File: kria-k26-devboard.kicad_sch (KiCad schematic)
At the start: 6 parts

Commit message: initial fork commit.
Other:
- sheet I2C  renamed I2C
- sheet PCIE M2 key E  renamed PCIE M2 key E

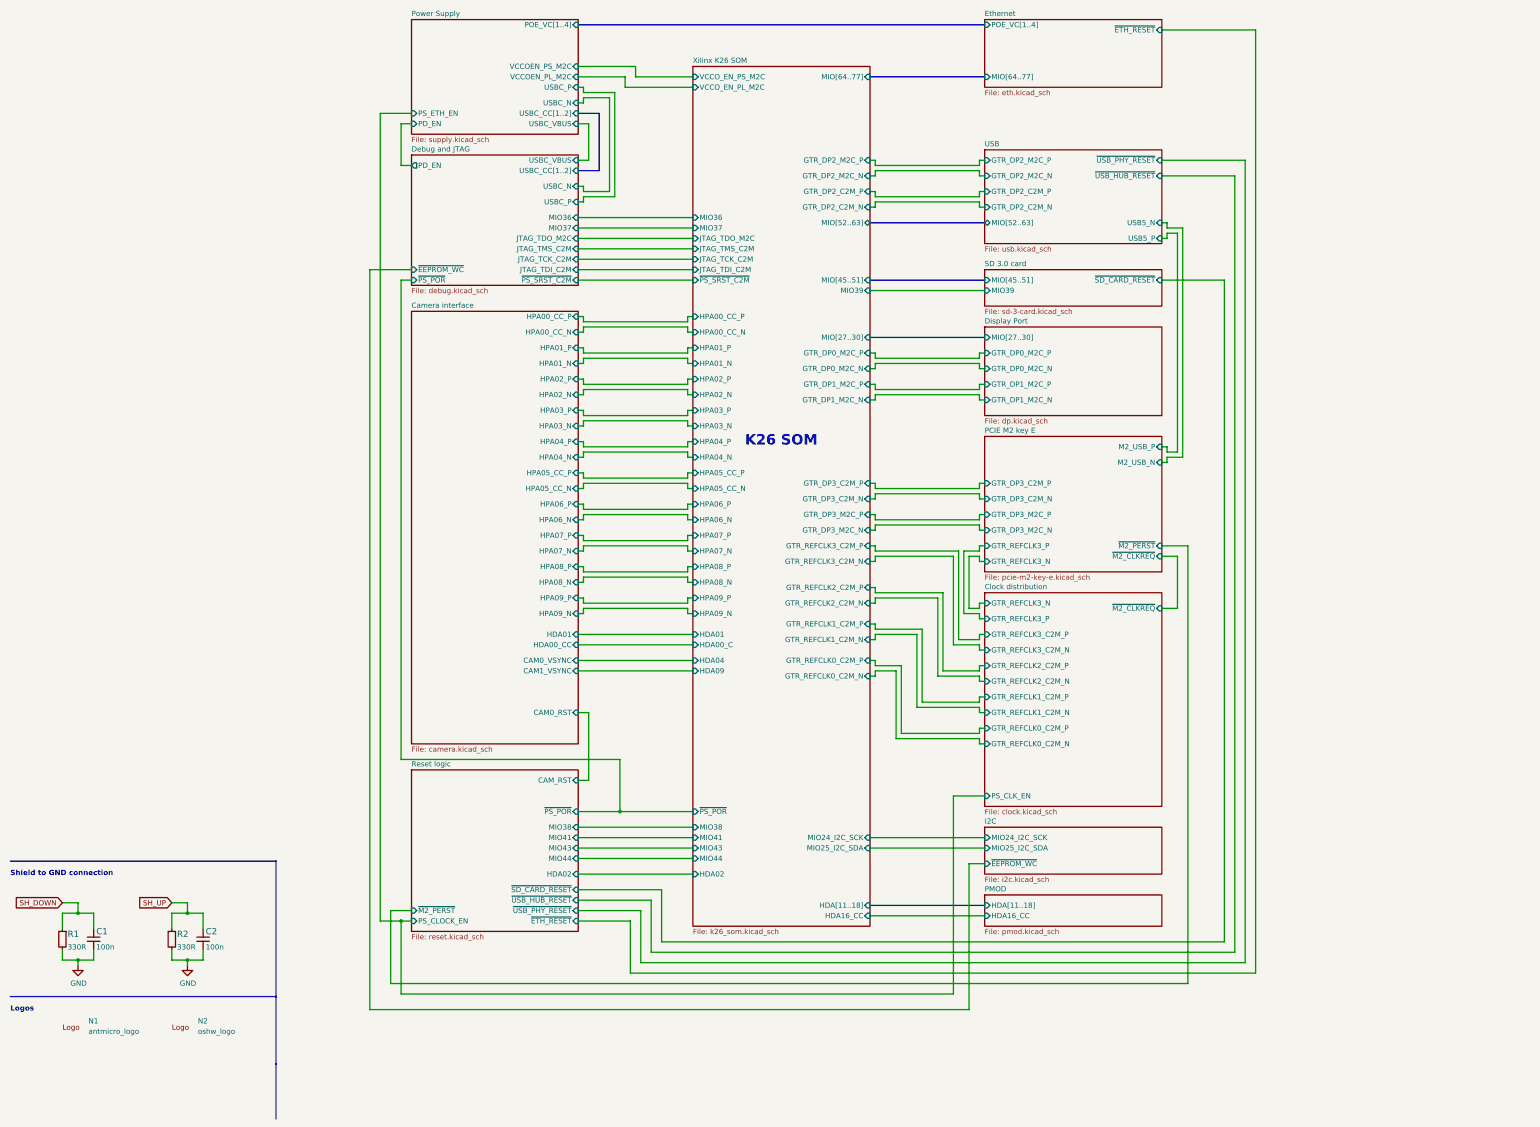
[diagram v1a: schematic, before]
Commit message: post-cut, added second set of mezzanine connectors.
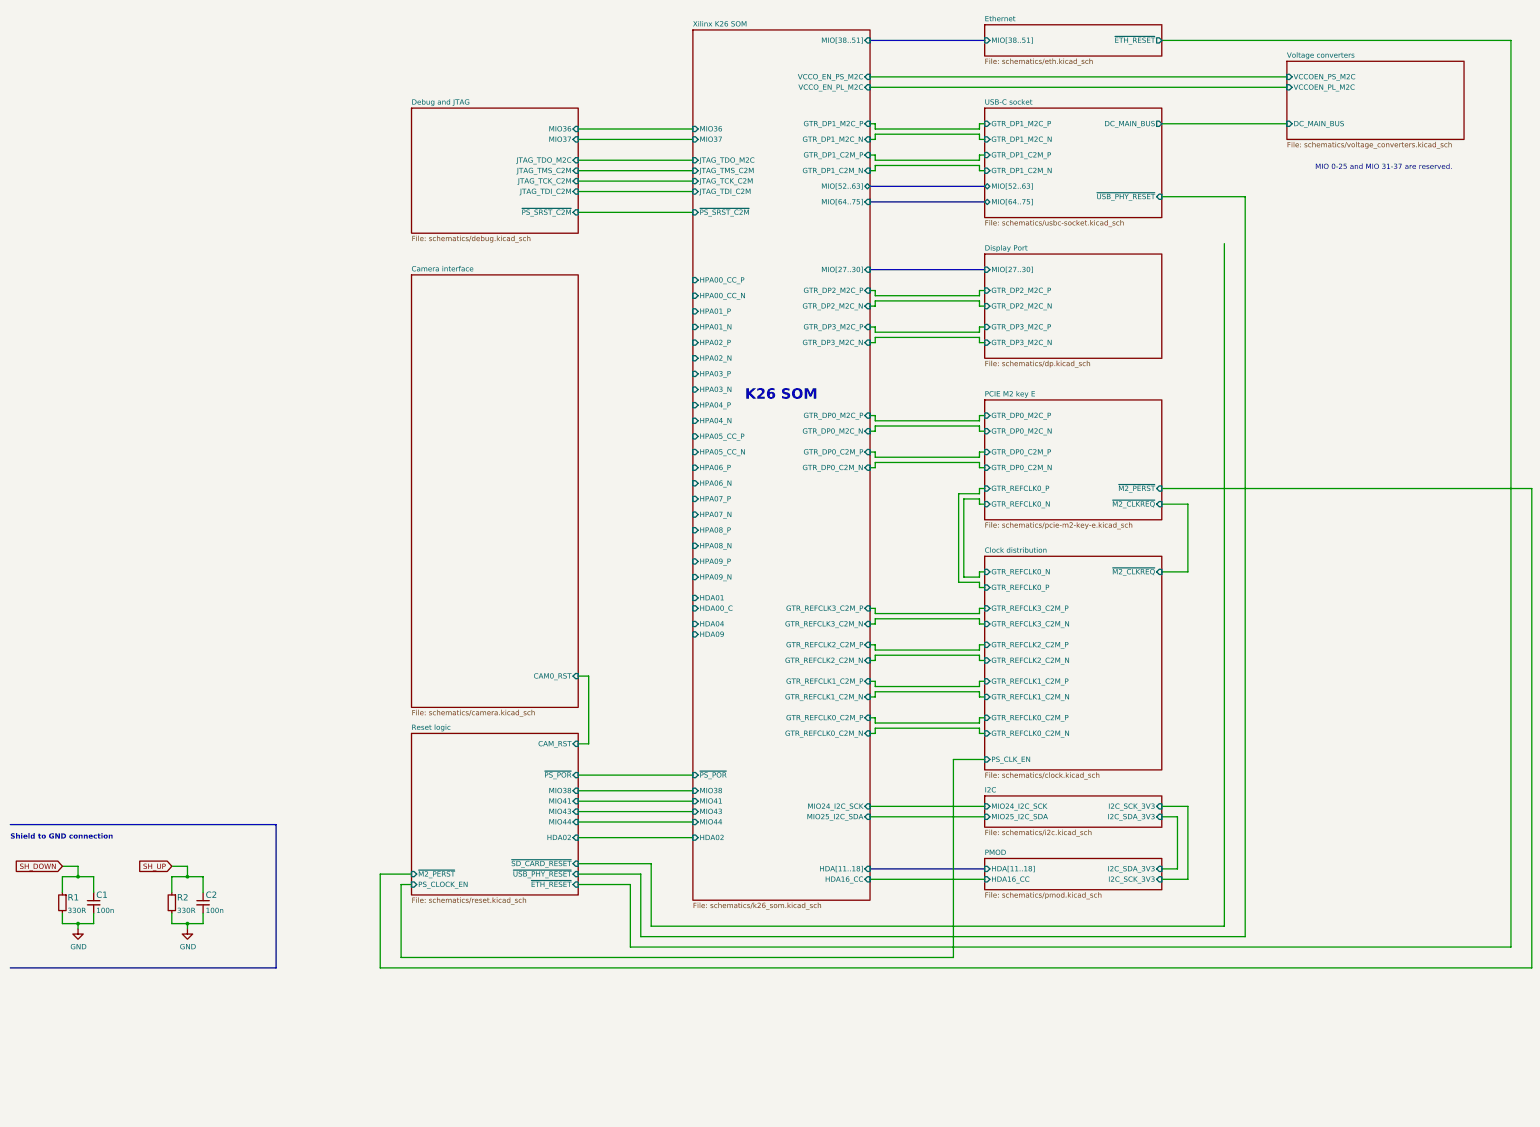
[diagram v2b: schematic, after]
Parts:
- removed N1: antmicro_logo, kria-k26-devboard-footprints:antmicro-logo, symbol kria-k26-devboard:antmicro_logo
- removed N2: oshw_logo, kria-k26-devboard-footprints:oshw-logo, symbol kria-k26-devboard:oshw_logo
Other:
- sheet USB renamed USB-C socket
- removed sheet Power Supply
- removed sheet SD 3.0 card
- added sheet Voltage converters (schematics/voltage_converters.kicad_sch)
- sheet Camera interface: file camera.kicad_sch -> schematics/camera.kicad_sch
- sheet Camera interface ports: added none; removed CAM0_VSYNC, CAM1_VSYNC, HDA00_CC, HDA01, HPA00_CC_N, HPA00_CC_P, HPA01_N, HPA01_P, HPA02_N, HPA02_P, HPA03_N, HPA03_P, HPA04_N, HPA04_P, HPA05_CC_N, HPA05_CC_P, HPA06_N, HPA06_P, HPA07_N, HPA07_P, HPA08_N, HPA08_P, HPA09_N, HPA09_P
- sheet Clock distribution: file clock.kicad_sch -> schematics/clock.kicad_sch
- sheet Clock distribution ports: added GTR_REFCLK0_N, GTR_REFCLK0_P; removed GTR_REFCLK3_N, GTR_REFCLK3_P
- sheet Debug and JTAG: file debug.kicad_sch -> schematics/debug.kicad_sch
- sheet Debug and JTAG ports: added none; removed PD_EN, USBC_CC[1..2], USBC_N, USBC_P, USBC_VBUS, ~{EEPROM_WC}, ~{PS_POR}
- sheet Display Port: file dp.kicad_sch -> schematics/dp.kicad_sch
- sheet Display Port ports: added GTR_DP2_M2C_N, GTR_DP2_M2C_P, GTR_DP3_M2C_N, GTR_DP3_M2C_P; removed GTR_DP0_M2C_N, GTR_DP0_M2C_P, GTR_DP1_M2C_N, GTR_DP1_M2C_P
- sheet Ethernet: file eth.kicad_sch -> schematics/eth.kicad_sch
- sheet Ethernet ports: added MIO[38..51]; removed MIO[64..77], POE_VC[1..4]
- sheet I2C: file i2c.kicad_sch -> schematics/i2c.kicad_sch
- sheet I2C ports: added I2C_SCK_3V3, I2C_SDA_3V3; removed ~{EEPROM_WC}
- sheet PCIE M2 key E: file pcie-m2-key-e.kicad_sch -> schematics/pcie-m2-key-e.kicad_sch
- sheet PCIE M2 key E ports: added GTR_DP0_C2M_N, GTR_DP0_C2M_P, GTR_DP0_M2C_N, GTR_DP0_M2C_P, GTR_REFCLK0_N, GTR_REFCLK0_P; removed GTR_DP3_C2M_N, GTR_DP3_C2M_P, GTR_DP3_M2C_N, GTR_DP3_M2C_P, GTR_REFCLK3_N, GTR_REFCLK3_P, M2_USB_N, M2_USB_P
- sheet PMOD: file pmod.kicad_sch -> schematics/pmod.kicad_sch
- sheet PMOD ports: added I2C_SCK_3V3, I2C_SDA_3V3; removed none
- sheet Reset logic: file reset.kicad_sch -> schematics/reset.kicad_sch
- sheet Reset logic ports: added none; removed ~{USB_HUB_RESET}
- sheet USB-C socket: file usb.kicad_sch -> schematics/usbc-socket.kicad_sch
- sheet USB-C socket ports: added DC_MAIN_BUS, GTR_DP1_C2M_N, GTR_DP1_C2M_P, GTR_DP1_M2C_N, GTR_DP1_M2C_P, MIO[64..75]; removed GTR_DP2_C2M_N, GTR_DP2_C2M_P, GTR_DP2_M2C_N, GTR_DP2_M2C_P, USB5_N, USB5_P, ~{USB_HUB_RESET}
- sheet Xilinx K26 SOM: file k26_som.kicad_sch -> schematics/k26_som.kicad_sch
- sheet Xilinx K26 SOM ports: added GTR_DP0_C2M_N, GTR_DP0_C2M_P, GTR_DP1_C2M_N, GTR_DP1_C2M_P, MIO[38..51], MIO[64..75]; removed GTR_DP2_C2M_N, GTR_DP2_C2M_P, GTR_DP3_C2M_N, GTR_DP3_C2M_P, MIO39, MIO[45..51], MIO[64..77]
- note added: "MIO 0-25 and MIO 31-37 are reserved."
- note removed: "Logos"
- moved on the sheet: C1, C2, R1, R2

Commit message: Voltage converter added
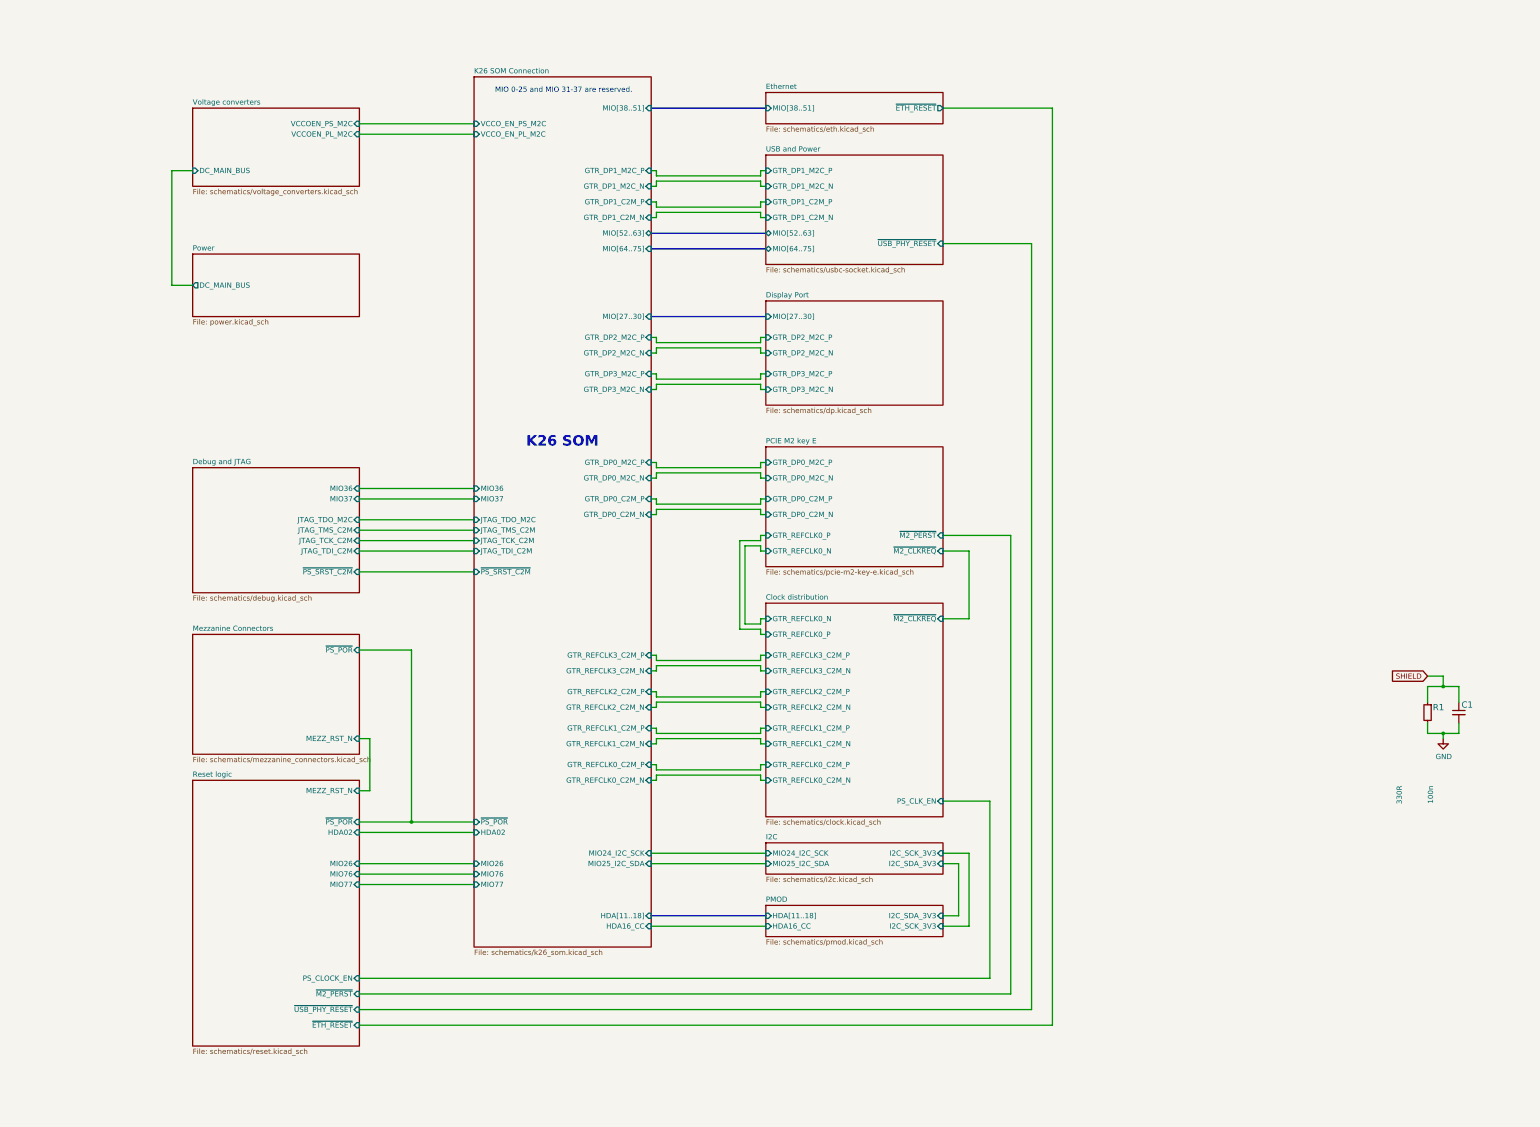
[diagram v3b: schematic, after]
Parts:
- removed C2: C_100n_0402, kria-k26-devboard-footprints:C_0402_1005Metric, symbol kria-k26-devboard:C_100n_0402
- removed R2: R_330R_0402, kria-k26-devboard-footprints:R_0402_1005Metric, symbol kria-k26-devboard:R_330R_0402
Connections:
- net SH_DOWN renamed SHIELD
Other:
- sheet Camera interface renamed Mezzanine Connectors
- sheet USB-C socket renamed USB and Power
- sheet Xilinx K26 SOM renamed K26 SOM Connection
- added sheet Power (power.kicad_sch)
- sheet K26 SOM Connection ports: added MIO26, MIO76, MIO77; removed HDA00_C, HDA01, HDA04, HDA09, HPA00_CC_N, HPA00_CC_P, HPA01_N, HPA01_P, HPA02_N, HPA02_P, HPA03_N, HPA03_P, HPA04_N, HPA04_P, HPA05_CC_N, HPA05_CC_P, HPA06_N, HPA06_P, HPA07_N, HPA07_P, HPA08_N, HPA08_P, HPA09_N, HPA09_P, MIO38, MIO41, MIO43, MIO44
- sheet Mezzanine Connectors: file schematics/camera.kicad_sch -> schematics/mezzanine_connectors.kicad_sch
- sheet Mezzanine Connectors ports: added MEZZ_RST_N, ~{PS_POR}; removed CAM0_RST
- sheet Reset logic ports: added MEZZ_RST_N, MIO26, MIO76, MIO77; removed CAM_RST, MIO38, MIO41, MIO43, MIO44, ~{SD_CARD_RESET}
- sheet USB and Power ports: added none; removed DC_MAIN_BUS
- note removed: "Shield to GND connection"
